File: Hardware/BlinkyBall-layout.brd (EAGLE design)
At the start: 27 parts, among them IC1 TINY13-20SSU, IC2 TINY13-20SSU, IC3 TINY13-20SSU, IC4 TINY13-20SSU, IC5 TINY13-20SSU, IC6 TINY13-20SSU, IC7 TINY13-20SSU, IC8 TINY13-20SSU, IC9 TINY13-20SSU

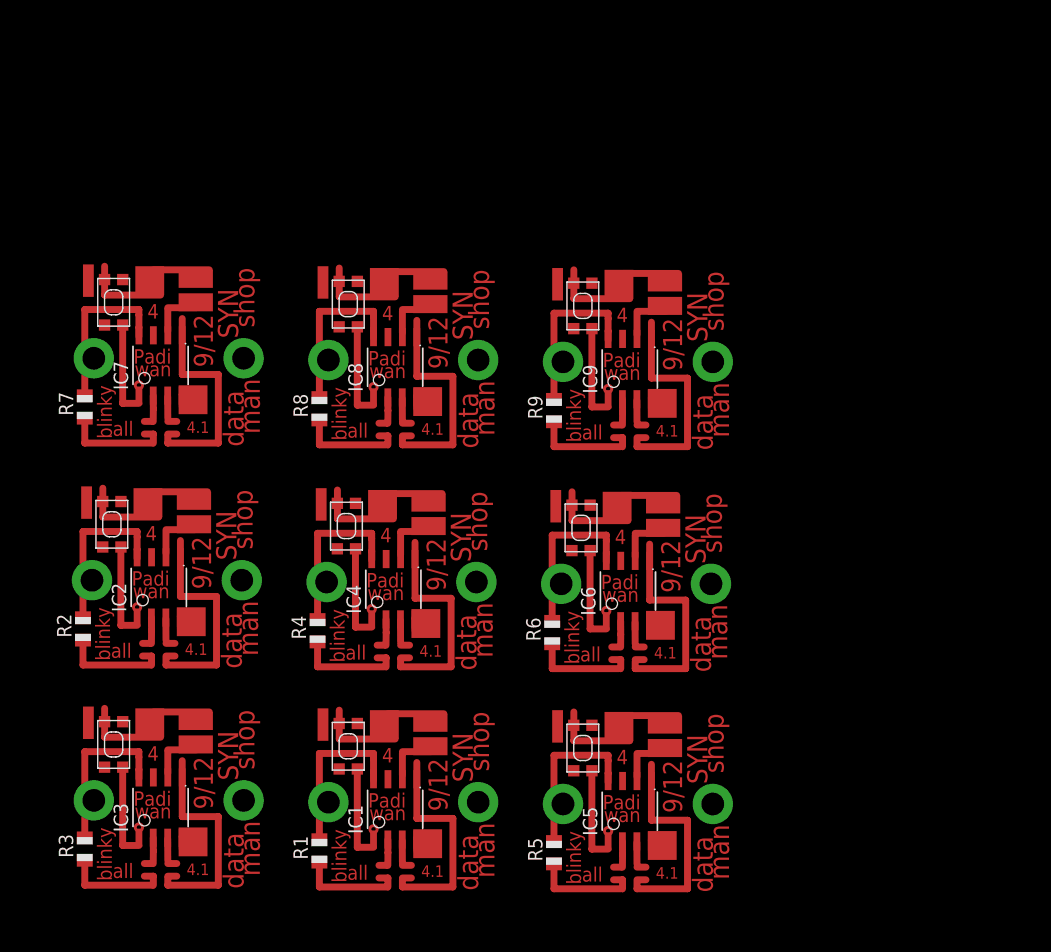
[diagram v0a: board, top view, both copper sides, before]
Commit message: Adjusting Layout, v4.2
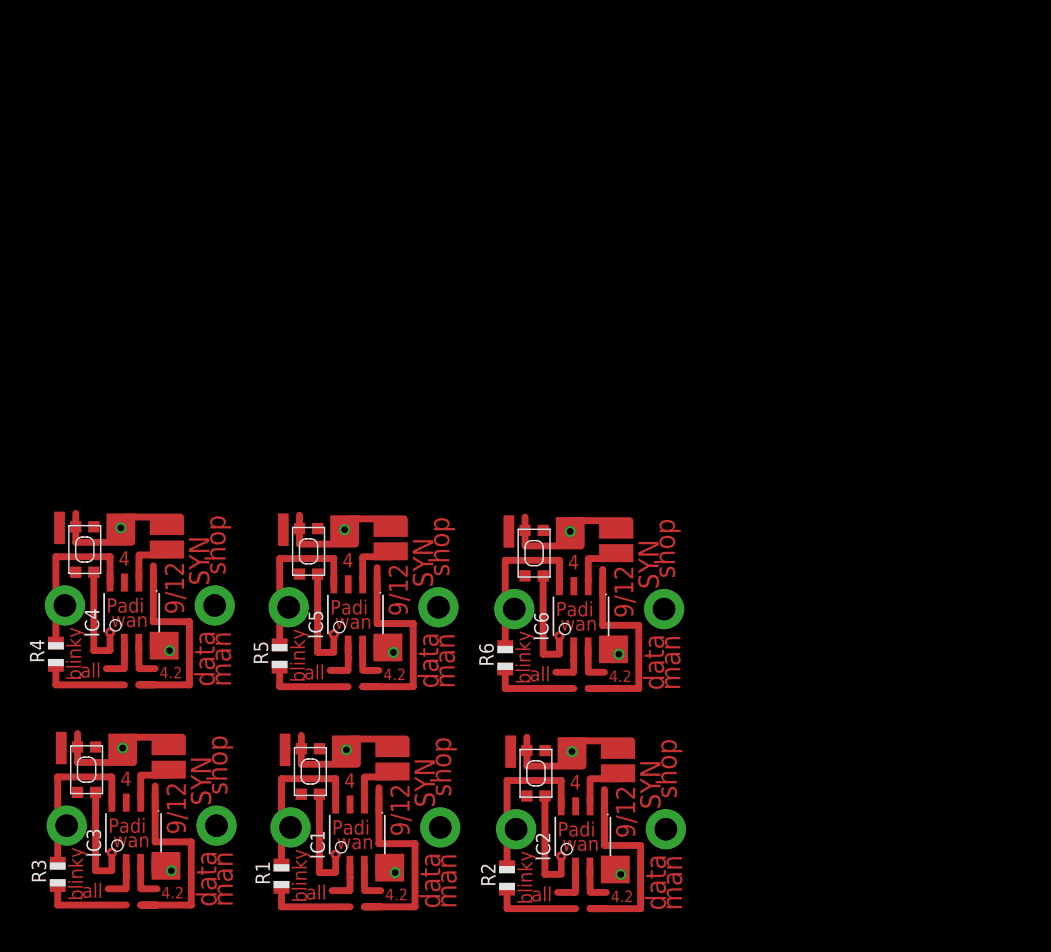
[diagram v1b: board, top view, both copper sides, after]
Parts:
- removed E$7, E$8, E$9: (no value), adafruit:KMR2
- removed IC7, IC8, IC9: TINY13-20SSU, atmel:8S1
- removed R7, R8, R9: (no value), adafruit:R0805
- moved E$3 43.3 mm to (43.0, 12.4)
- moved IC2 43.3 mm to (47.1, 6.83)
- moved R2 43.3 mm to (40.5, 3.17)
- moved E$5 29.7 mm to (23.0, 31.9)
- moved IC5 29.7 mm to (27.1, 26.4)
- moved R5 29.7 mm to (20.5, 22.7)
- moved IC4 23.1 mm to (7.46, 26.5)
- moved R4 23.1 mm to (0.79, 22.9)
- moved E$4 23.1 mm to (3.33, 32.1)
- moved R6 4.69 mm to (40.3, 22.5)
- moved E$6 4.69 mm to (42.9, 31.8)
- moved IC6 4.69 mm to (47.0, 26.2)
- moved E$1 4.01 mm to (23.2, 12.5)
- moved IC1 4.01 mm to (27.3, 6.99)
- moved R1 4.01 mm to (20.6, 3.33)
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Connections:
- removed net N$32: IC7.5
- removed net N$33: IC7.2
- removed net N$34: IC7.3
- removed net N$35: R7.1
- removed net N$36: IC7.4, R7.2
- removed net N$37: IC8.5
- removed net N$38: IC8.2
- removed net N$40: IC8.3
- removed net N$41: R8.1
- removed net N$42: IC8.4, R8.2
- removed net N$43: IC9.5
- removed net N$44: IC9.2
- removed net N$45: IC9.3
- removed net N$46: R9.1
- removed net N$47: IC9.4, R9.2
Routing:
- net S$54: track 19.2 -> 0.00 mm, vias 0 -> 2
- net S$102: track 19.2 -> 0.00 mm
- net S$78: track 19.2 -> 0.00 mm, vias 0 -> 1
- net S$90: track 19.2 -> 0.00 mm
- net S$32: track 0.63 -> 18.1 mm
- net S$18: track 19.2 -> 1.75 mm
- net S$45: track 1.59 -> 18.1 mm
- net S$19: track 1.90 -> 18.1 mm
- net S$71: track 2.54 -> 18.1 mm
- net S$66: track 19.2 -> 6.35 mm
- net S$30: track 19.2 -> 8.26 mm
- net S$58: track 7.46 -> 18.1 mm
- net S$99: track 10.0 -> 0.00 mm
- net S$39: track 10.0 -> 0.00 mm, vias 0 -> 1
- net S$51: track 10.0 -> 0.00 mm, vias 0 -> 1
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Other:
- board text added: "4.2"
- board text removed: "4.1"

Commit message: Final Board Adjustments?
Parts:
- added E$10, E$11, E$12, E$13, E$14, E$15, E$16, E$7, E$8, E$9: (no value), adafruit:KMR2
- added IC10, IC11, IC12, IC13, IC14, IC15, IC16, IC7, IC8, IC9: TINY13-20SSU, atmel:8S1
- added R10, R11, R12, R13, R14, R15, R16, R7, R8, R9: (no value), adafruit:R0805
- moved E$4 70.4 mm to (71.3, 13.5)
- moved IC4 70.4 mm to (75.4, 7.94)
- moved R4 70.4 mm to (68.7, 4.29)
- moved E$5 19.6 mm to (3.49, 33.2)
- moved R5 19.6 mm to (0.95, 24.0)
- moved IC5 19.6 mm to (7.62, 27.6)
- moved IC6 16.9 mm to (30.2, 27.8)
- moved E$6 16.9 mm to (26.0, 33.3)
- moved R6 16.9 mm to (23.5, 24.1)
- moved E$3 5.61 mm to (48.6, 13.2)
- moved IC2 5.61 mm to (52.7, 7.62)
- moved R2 5.61 mm to (46.0, 3.97)
- moved E$1 2.74 mm to (25.9, 13.0)
- moved IC1 2.74 mm to (30.0, 7.46)
- moved R1 2.74 mm to (23.3, 3.81)
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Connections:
- new net N$32: IC7.5
- new net N$33: IC7.2
- new net N$34: IC7.3
- new net N$35: R7.1
- new net N$36: IC7.4, R7.2
- new net N$37: IC8.5
- new net N$38: IC8.2
- new net N$40: IC8.3
- new net N$41: R8.1
- new net N$42: IC8.4, R8.2
- new net N$43: IC9.5
- new net N$44: IC9.2
- new net N$45: IC9.3
- new net N$46: R9.1
- new net N$47: IC9.4, R9.2
- new net N$48: IC10.5
- new net N$49: IC10.2
- new net N$50: IC10.3
- new net N$51: R10.1
- new net N$52: IC10.4, R10.2
- new net N$53: IC11.5
- new net N$54: IC11.2
- new net N$55: IC11.3
- new net N$56: R11.1
- new net N$57: IC11.4, R11.2
- new net N$58: IC12.5
- new net N$59: IC12.2
- new net N$60: IC12.3
- new net N$61: R12.1
- new net N$62: IC12.4, R12.2
- new net N$63: IC13.5
- new net N$64: IC13.2
- new net N$65: IC13.3
- new net N$66: R13.1
- new net N$67: IC13.4, R13.2
- new net N$68: IC14.5
- new net N$69: IC14.2
- new net N$70: IC14.3
- new net N$71: R14.1
- new net N$72: IC14.4, R14.2
- new net N$73: IC15.5
- new net N$74: IC15.2
- new net N$75: IC15.3
- new net N$76: R15.1
- new net N$77: IC15.4, R15.2
- new net N$78: IC16.5
- new net N$79: IC16.2
- new net N$80: IC16.3
- new net N$81: R16.1
- new net N$82: IC16.4, R16.2
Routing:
- net S$188: track 0.00 -> 18.1 mm
- net S$84: track 0.00 -> 18.1 mm
- net S$123: track 0.00 -> 18.1 mm
- net S$175: track 0.00 -> 18.1 mm
- net S$136: track 0.00 -> 18.1 mm
- net S$110: track 0.00 -> 18.1 mm
- net S$162: track 0.00 -> 18.1 mm
- net S$97: track 0.00 -> 18.1 mm
- net S$201: track 0.00 -> 18.1 mm
- net S$149: track 0.00 -> 18.1 mm
- net S$198: track 0.00 -> 10.0 mm
- net S$185: track 0.00 -> 10.0 mm
- net S$94: track 0.00 -> 10.0 mm
- net S$146: track 0.00 -> 10.0 mm
- net S$120: track 0.00 -> 10.0 mm
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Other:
- board text added: "4.3"
- board text added: "hop"
- board text removed: "4"
- board text removed: "4.2"
- board text removed: "shop"
